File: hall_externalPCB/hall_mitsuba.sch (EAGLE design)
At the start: 7 parts, among them J1 HEADER_SIDE_5POS, U1 HALLSOT23W, U2 HALLSOT23W, U3 HALLSOT23W

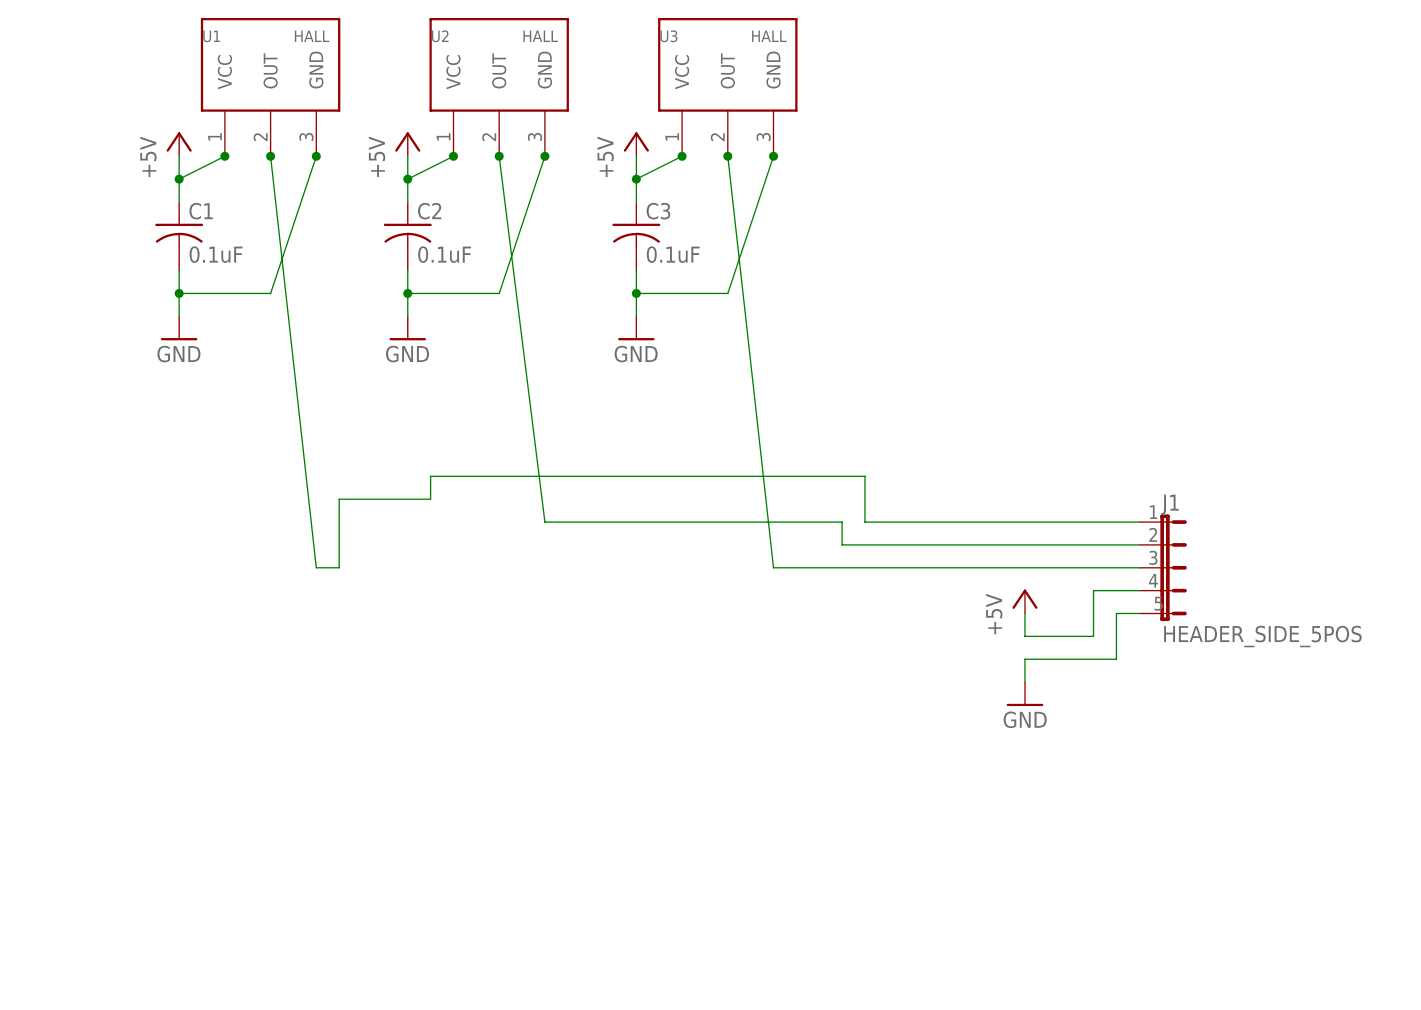
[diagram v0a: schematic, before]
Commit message: placed 8-pin connector
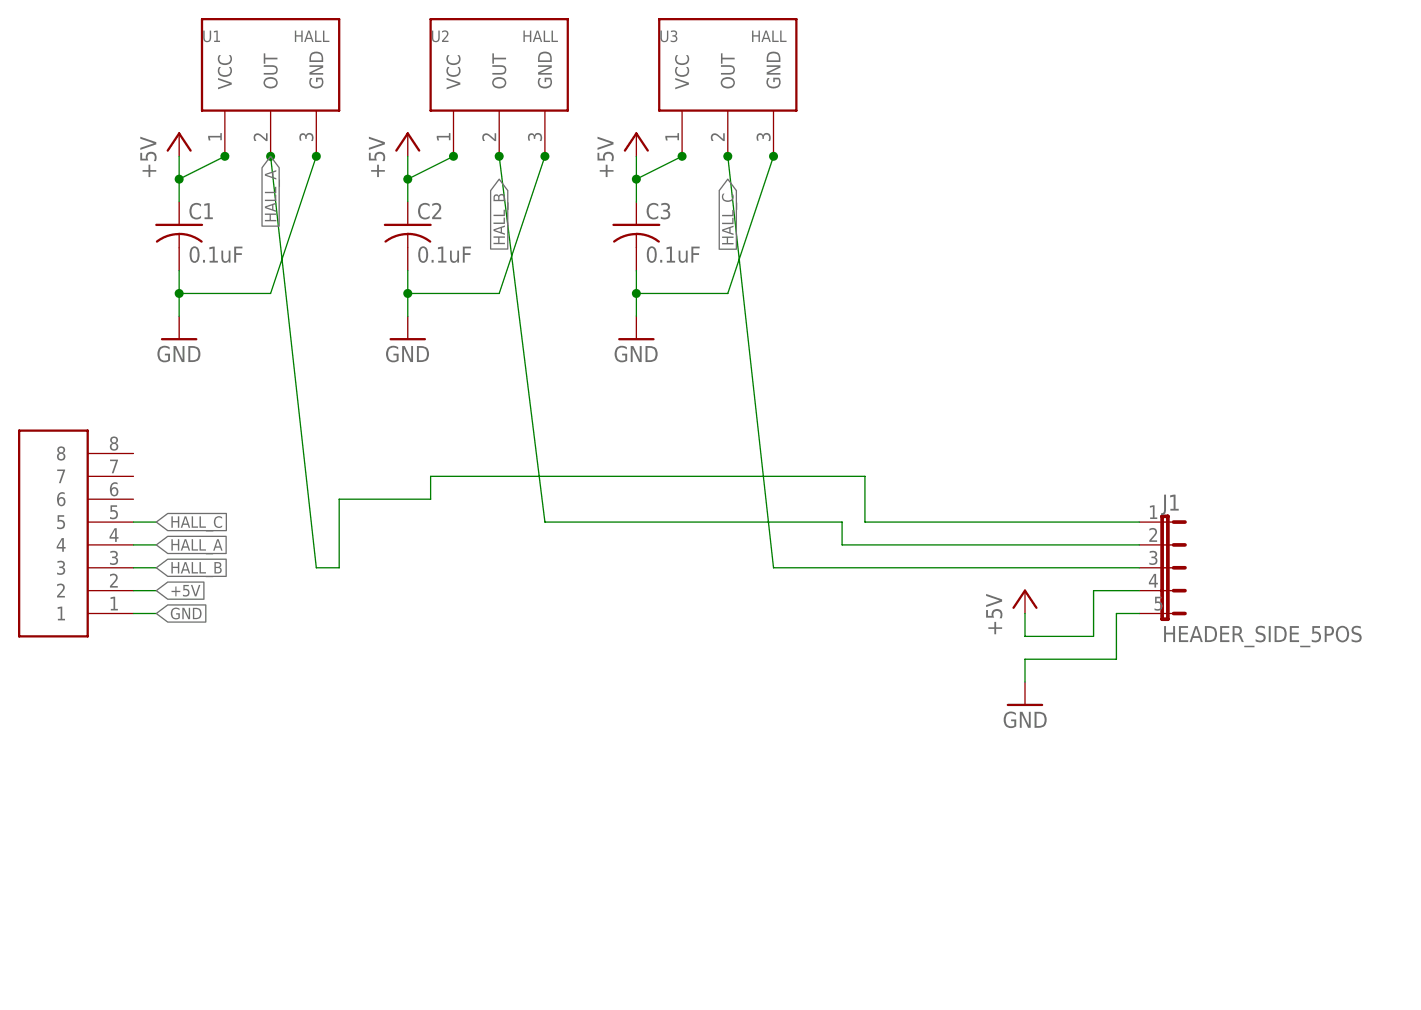
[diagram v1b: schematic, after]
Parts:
- added U$1: HEADER8DEFAULT, Custom_new:HEADER8DEFAULT
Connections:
- removed net N$2: J1.1, U1.OUT
- removed net N$4: J1.3, U3.OUT
- removed net N$7: J1.2, U2.OUT
- new net HALL_A: J1.1, U$1.4, U1.OUT
- new net HALL_B: J1.2, U$1.3, U2.OUT
- new net HALL_C: J1.3, U$1.5, U3.OUT
- net +5V: now also U$1.2
- net GND: now also U$1.1
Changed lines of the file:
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@@
 <part name="GND4" library="supply1" deviceset="GND" device=""/>
 <part name="J1" library="sc_usercreated" deviceset="HEADER_SIDE_5POS" device=""/>
+<part name="U$1" library="Custom_new" deviceset="HEADER8" device="DEFAULT"/>
 </parts>
 <sheets>
@@
 <instance part="GND4" gate="1" x="99.06" y="0" rot="MR0"/>
 <instance part="J1" gate="G$1" x="114.3" y="15.24" rot="R270"/>
+<instance part="U$1" gate="G$1" x="-7.62" y="17.78"/>
 </instances>
 <busses>
@@
 <pinref part="P+4" gate="1" pin="+5V"/>
 <pinref part="J1" gate="G$1" pin="4"/>
+</segment>
+<segment>
+<pinref part="U$1" gate="G$1" pin="2"/>
+<wire x1="0" y1="12.7" x2="2.54" y2="12.7" width="0.1524" layer="91"/>
+<label x="2.54" y="12.7" size="1.27" layer="95" xref="yes"/>
 </segment>
 </net>
@@
 <pinref part="GND4" gate="1" pin="GND"/>
 </segment>
+<segment>
+<pinref part="U$1" gate="G$1" pin="1"/>
+<wire x1="0" y1="10.16" x2="2.54" y2="10.16" width="0.1524" layer="91"/>
+<label x="2.54" y="10.16" size="1.27" layer="95" xref="yes"/>
+</segment>
 </net>
-<net name="N$2" class="0">
+<net name="HALL_B" class="0">
+<segment>
+<pinref part="U$1" gate="G$1" pin="3"/>
+<wire x1="0" y1="15.24" x2="2.54" y2="15.24" width="0.1524" layer="91"/>
+<label x="2.54" y="15.24" size="1.27" layer="95" xref="yes"/>
+</segment>
+<segment>
+<wire x1="45.72" y1="20.32" x2="40.64" y2="60.96" width="0.1524" layer="91"/>
+<wire x1="78.74" y1="17.78" x2="111.76" y2="17.78" width="0.1524" layer="91"/>
+<wire x1="45.72" y1="20.32" x2="78.74" y2="20.32" width="0.1524" layer="91"/>
+<wire x1="78.74" y1="20.32" x2="78.74" y2="17.78" width="0.1524" layer="91"/>
+<junction x="40.64" y="60.96"/>
+<pinref part="U2" gate="G$1" pin="OUT"/>
+<pinref part="J1" gate="G$1" pin="2"/>
+<label x="40.64" y="58.42" size="1.27" layer="95" rot="R270" xref="yes"/>
+</segment>
+</net>
+<net name="HALL_A" class="0">
+<segment>
+<pinref part="U$1" gate="G$1" pin="4"/>
+<wire x1="0" y1="17.78" x2="2.54" y2="17.78" width="0.1524" layer="91"/>
+<label x="2.54" y="17.78" size="1.27" layer="95" xref="yes"/>
+</segment>
 <segment>
 <wire x1="15.24" y1="60.96" x2="20.32" y2="15.24" width="0.1524" layer="91"/>
@@
 <pinref part="U1" gate="G$1" pin="OUT"/>
 <pinref part="J1" gate="G$1" pin="1"/>
+<label x="15.24" y="60.96" size="1.27" layer="95" rot="R270" xref="yes"/>
 </segment>
 </net>
-<net name="N$4" class="0">
+<net name="HALL_C" class="0">
+<segment>
+<pinref part="U$1" gate="G$1" pin="5"/>
+<wire x1="0" y1="20.32" x2="2.54" y2="20.32" width="0.1524" layer="91"/>
+<label x="2.54" y="20.32" size="1.27" layer="95" xref="yes"/>
+</segment>
 <segment>
 <wire x1="66.04" y1="60.96" x2="71.12" y2="15.24" width="0.1524" layer="91"/>
@@
 <pinref part="U3" gate="G$1" pin="OUT"/>
 <pinref part="J1" gate="G$1" pin="3"/>
+<label x="66.04" y="58.42" size="1.27" layer="95" rot="R270" xref="yes"/>
 </segment>
 </net>
-<net name="N$7" class="0">
-<segment>
-<wire x1="45.72" y1="20.32" x2="40.64" y2="60.96" width="0.1524" layer="91"/>
-<wire x1="78.74" y1="17.78" x2="111.76" y2="17.78" width="0.1524" layer="91"/>
-<wire x1="45.72" y1="20.32" x2="78.74" y2="20.32" width="0.1524" layer="91"/>
-<wire x1="78.74" y1="20.32" x2="78.74" y2="17.78" width="0.1524" layer="91"/>
-<junction x="40.64" y="60.96"/>
-<pinref part="U2" gate="G$1" pin="OUT"/>
-<pinref part="J1" gate="G$1" pin="2"/>
-</segment>
-</net>

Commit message: routed halls - TODO: sensorless voltage dividers
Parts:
- removed J1: HEADER_SIDE_5POS, sc_usercreated:HEADER_SIDE_5POS
- added C4, C5, C6: (no value), SparkFun-Passives:CAP0603-CAP
- added R1, R2, R3, R4, R5, R6: (no value), SparkFun-Passives:RESISTOR0603-RES
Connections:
- new net HALL_A_RAW: R4.2, U1.OUT
- new net HALL_B_RAW: R5.2, U2.OUT
- new net HALL_C_RAW: R6.2, U3.OUT
- net +5V: now also R1.2, R2.2, R3.2; no longer J1.4
- net GND: now also C4.2, C5.2, C6.2; no longer J1.5
- net HALL_A: now also C4.1, R1.1, R4.1; no longer J1.1, U1.OUT
- net HALL_B: now also C5.1, R2.1, R5.1; no longer J1.2, U2.OUT
- net HALL_C: now also C6.1, R3.1, R6.1; no longer J1.3, U3.OUT

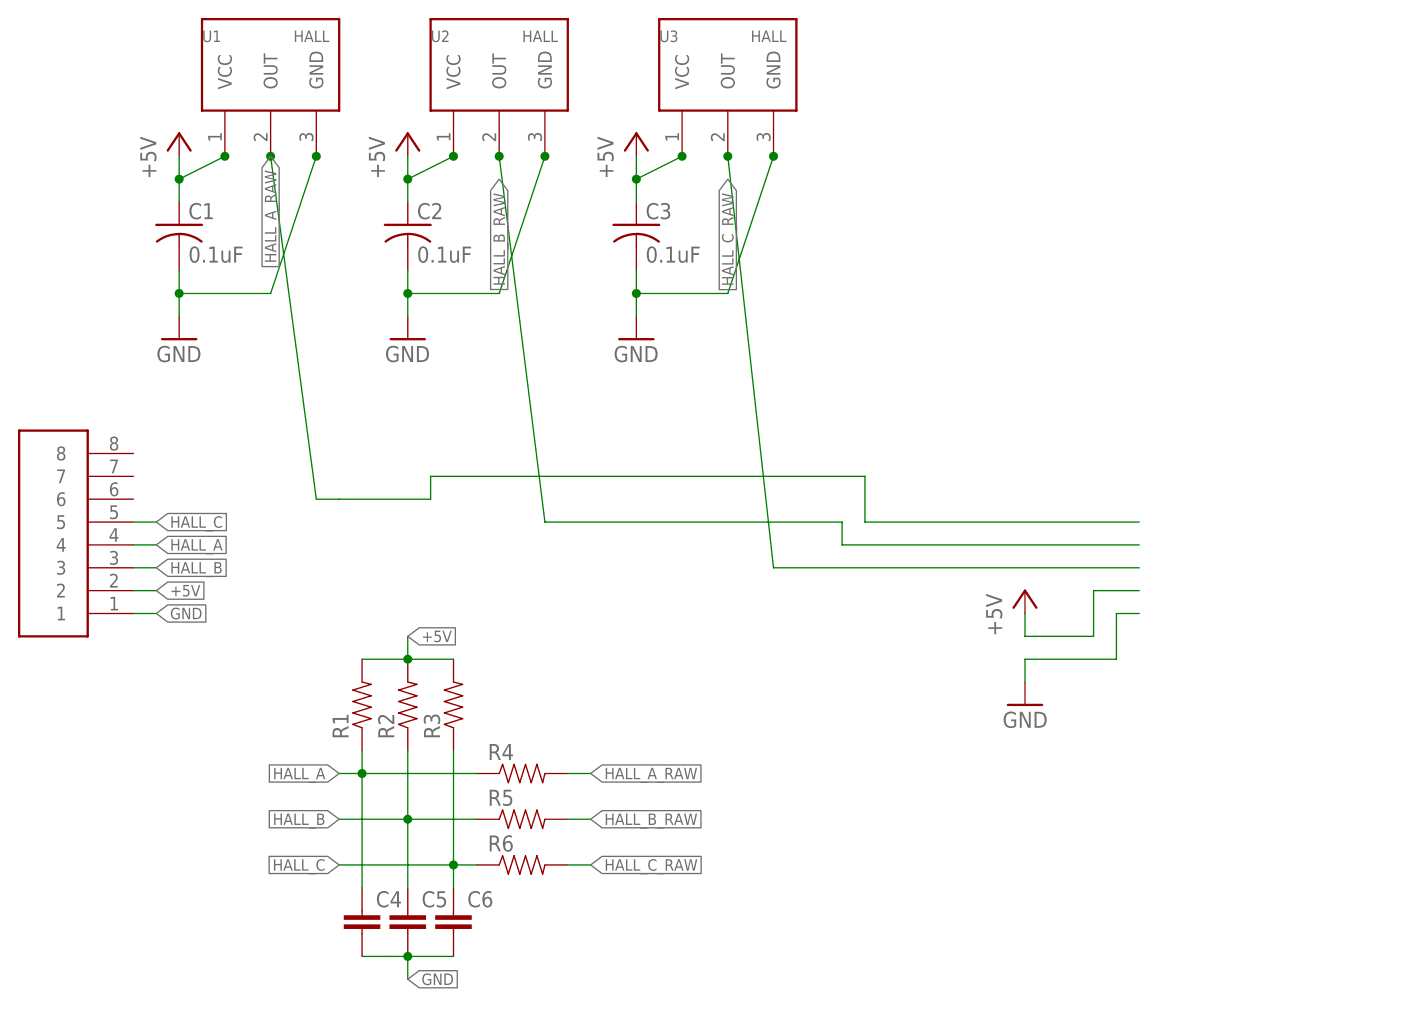
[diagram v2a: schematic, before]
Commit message: modified external hall mitsuba and also started on internal mitsuba controller
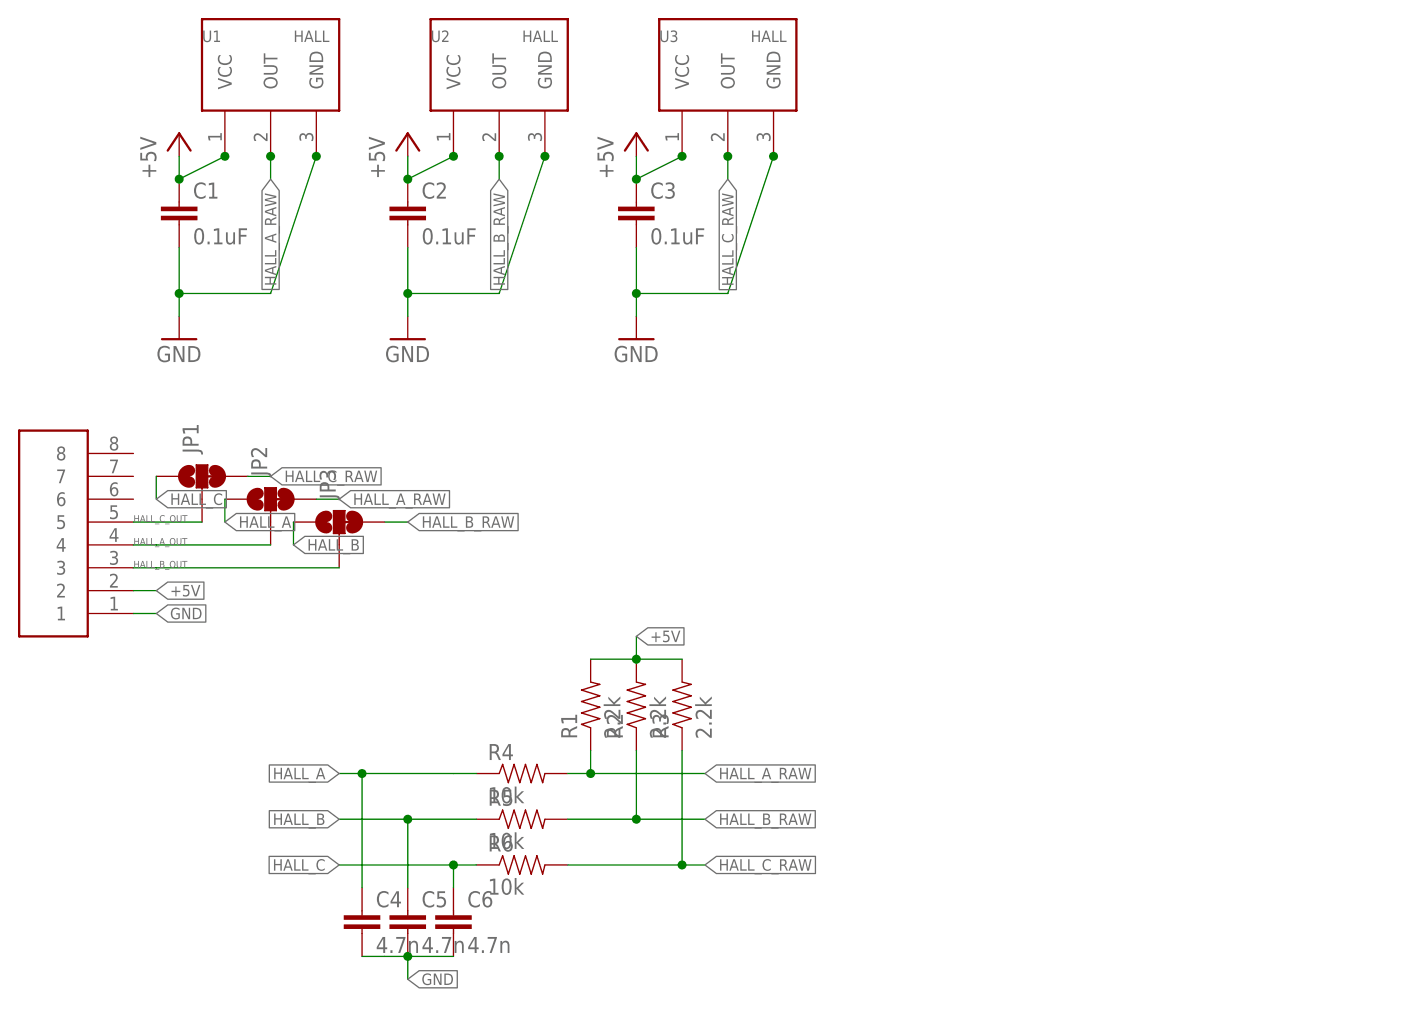
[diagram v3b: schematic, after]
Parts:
- added JP1, JP2, JP3: JUMPER-SMT_3_1-NC_TRACE_SILK, SparkFun-Jumpers:JUMPER-SMT_3_1-NC_TRACE_SILK
- C1, C2, C3: device rcl:C-USC0603 -> SparkFun-Passives:CAP0603-CAP
- C4, C5, C6: value (none) -> 4.7n
- R1, R2, R3: value (none) -> 2.2k
- R4, R5, R6: value (none) -> 10k
- U1, U2, U3: value HALLSOT23W -> HALL_SOT23W; device Custom_new:HALLSOT23W -> Custom_new:HALL_SOT23W
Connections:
- new net HALL_A_OUT: JP2.2, U$1.4
- new net HALL_B_OUT: JP3.2, U$1.3
- new net HALL_C_OUT: JP1.2, U$1.5
- net HALL_A: now also JP2.1; no longer R1.1, U$1.4
- net HALL_A_RAW: now also JP2.3, R1.1
- net HALL_B: now also JP3.1; no longer R2.1, U$1.3
- net HALL_B_RAW: now also JP3.3, R2.1
- net HALL_C: now also JP1.1; no longer R3.1, U$1.5
- net HALL_C_RAW: now also JP1.3, R3.1
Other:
- moved on the sheet: C1, C2, C3, R1, R2, R3
